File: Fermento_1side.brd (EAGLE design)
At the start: 85 x 68 mm, 25 parts, among them Q1 32.768kHz, Q2 P-MOSFET

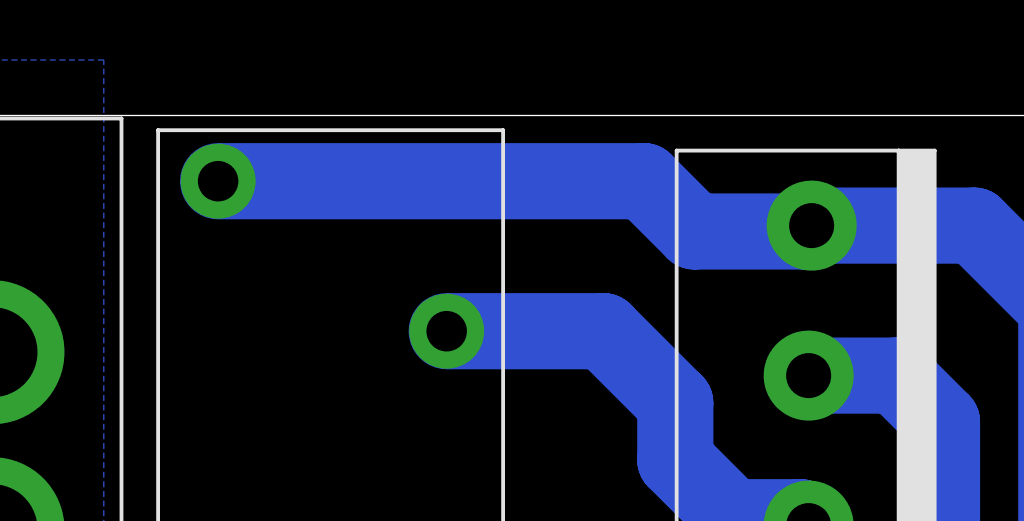
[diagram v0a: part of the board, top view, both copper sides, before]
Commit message: Added 1 sided version and png images.
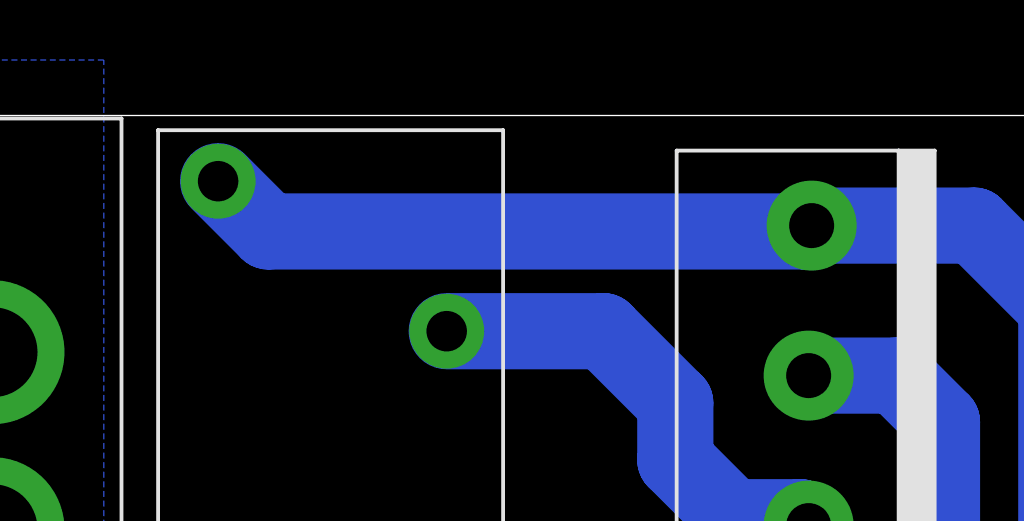
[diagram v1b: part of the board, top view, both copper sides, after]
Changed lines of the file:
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@@
 <wire x1="71.12" y1="44.45" x2="66.16" y2="44.45" width="2.54" layer="16"/>
 <wire x1="66.16" y1="44.45" x2="66.04" y2="44.33" width="2.54" layer="16"/>
-<wire x1="46.355" y1="65.81" x2="60.555" y2="65.81" width="2.54" layer="16"/>
-<wire x1="60.555" y1="65.81" x2="62.23" y2="64.135" width="2.54" layer="16"/>
-<wire x1="62.23" y1="64.135" x2="65.945" y2="64.135" width="2.54" layer="16"/>
 <wire x1="65.945" y1="64.135" x2="66.14" y2="64.33" width="2.54" layer="16"/>
 <wire x1="66.14" y1="64.33" x2="71.56" y2="64.33" width="2.54" layer="16"/>
+<wire x1="65.945" y1="64.135" x2="48.03" y2="64.135" width="2.54" layer="16"/>
+<wire x1="48.03" y1="64.135" x2="46.355" y2="65.81" width="2.54" layer="16"/>
 </signal>
 <signal name="N$8">

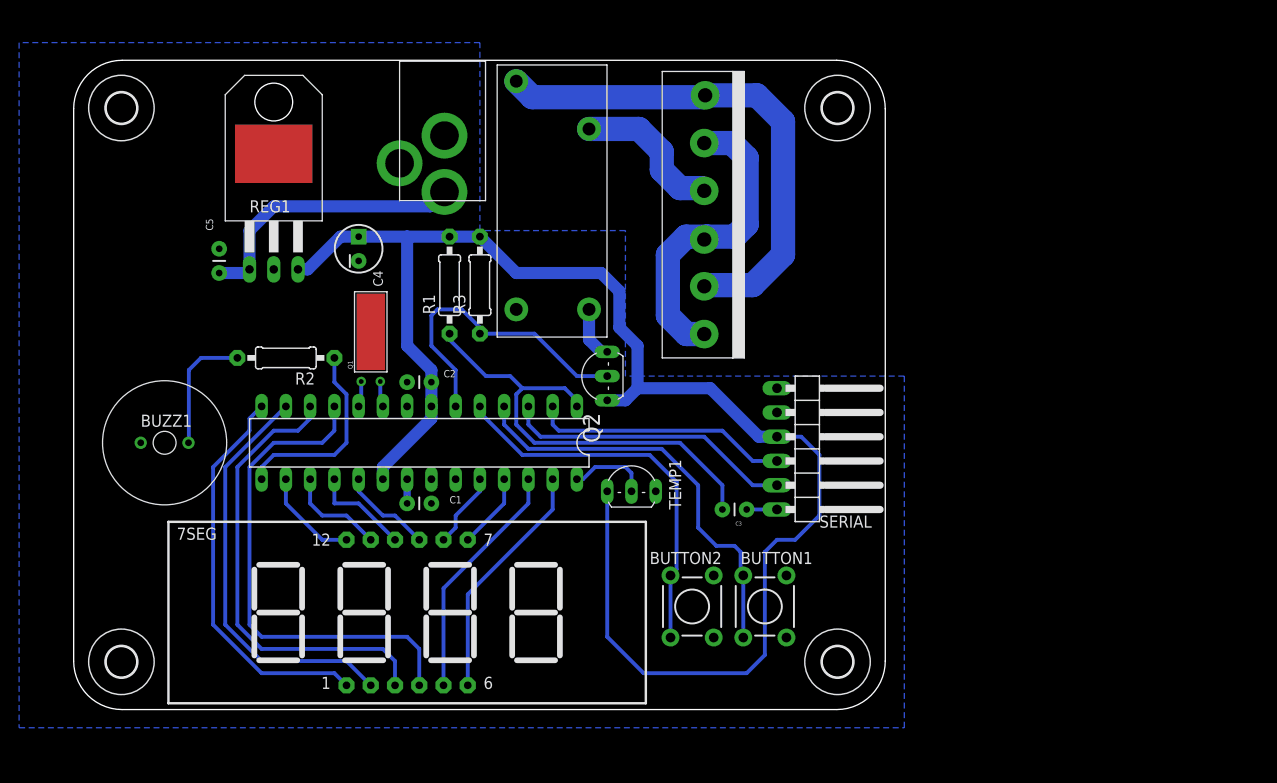
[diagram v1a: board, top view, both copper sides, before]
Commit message: Added mask and info diagram for 1sided homebrew incubator.
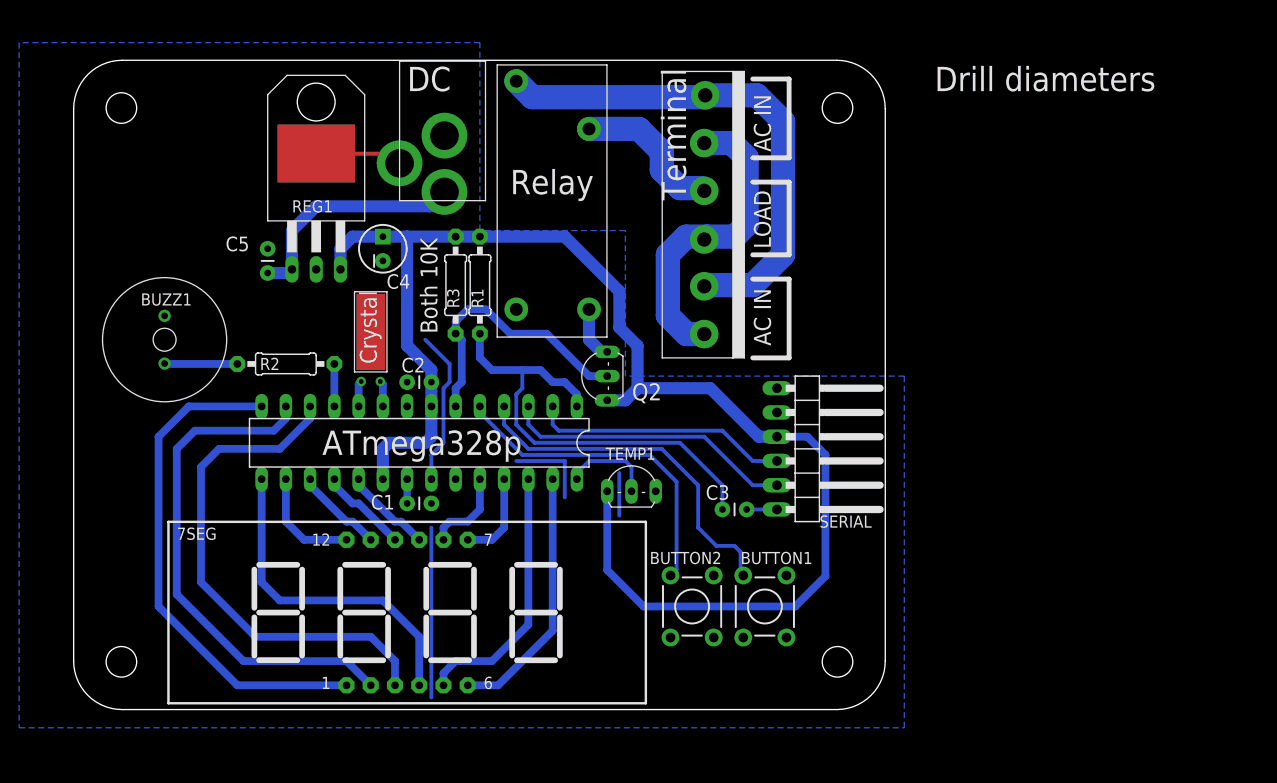
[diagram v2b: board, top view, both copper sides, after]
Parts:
- moved BUZZ1 10.8 mm to (9.53, 38.7), turned to 90 degrees
- moved C5 5.08 mm to (20.3, 45.7)
- moved REG1 4.45 mm to (20.3, 51.2)
- moved R1 3.18 mm to (42.5, 44.5)
- moved C4 2.54 mm to (32.4, 48.3)
- moved R3 2.54 mm to (40.0, 44.5)
- moved R2 0.63 mm to (22.2, 36.2)
- flipped H1 to the bottom
- flipped H2 to the bottom
- flipped H3 to the bottom
- flipped H4 to the bottom
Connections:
- net BUTTON1: no longer BUTTON1.1
- net BUTTON2: no longer BUTTON2.1
- net BUZZ: now also ATMEGA328.11; no longer ATMEGA328.15
- net C: now also ATMEGA328.15; no longer ATMEGA328.11
- net GND: no longer BUTTON1.3, BUTTON2.3
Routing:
- net GND: track 0.00 -> 56.7 mm
- net C: track 52.2 -> 34.8 mm
- net BUZZ: track 20.6 -> 4.45 mm
- net VCC: track 161.1 -> 149.0 mm
- net E: track 41.6 -> 53.0 mm
- net D: track 43.4 -> 53.5 mm
- net BUTTON2: track 40.8 -> 34.3 mm
- net BUTTON1: track 43.9 -> 37.4 mm
- net N$13: track 13.2 -> 7.64 mm
- net N$3: track 29.5 -> 24.4 mm
- net DP: track 48.1 -> 53.1 mm
- net AC_RELAY: track 32.5 -> 28.7 mm
- net G: track 25.3 -> 27.5 mm
- net DIG4: track 25.3 -> 27.1 mm
- net B: track 7.93 -> 9.42 mm
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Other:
- board text added: "AC IN"
- board text added: "ATmega328p"
- board text added: "All other drills: 0.9mm"
- board text added: "Both 10K"
- board text added: "Buttons: 1mm"
- board text added: "Buzzer+Crystal: 0.5mm"
- board text added: "Crystal"
- board text added: "DC"
- board text added: "DC Jack: 3mm"
- board text added: "Drill diameters"
- board text added: "LOAD"
- board text added: "Mount Holes: 3.2mm"
- board text added: "Regulator: 4mm"
- board text added: "Relay"
- board text added: "Relay: 1.35mm"
- board text added: "Terminal"
- board text added: "Terminal: 1.5mm"

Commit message: One sided homebrew-friendly design redone.
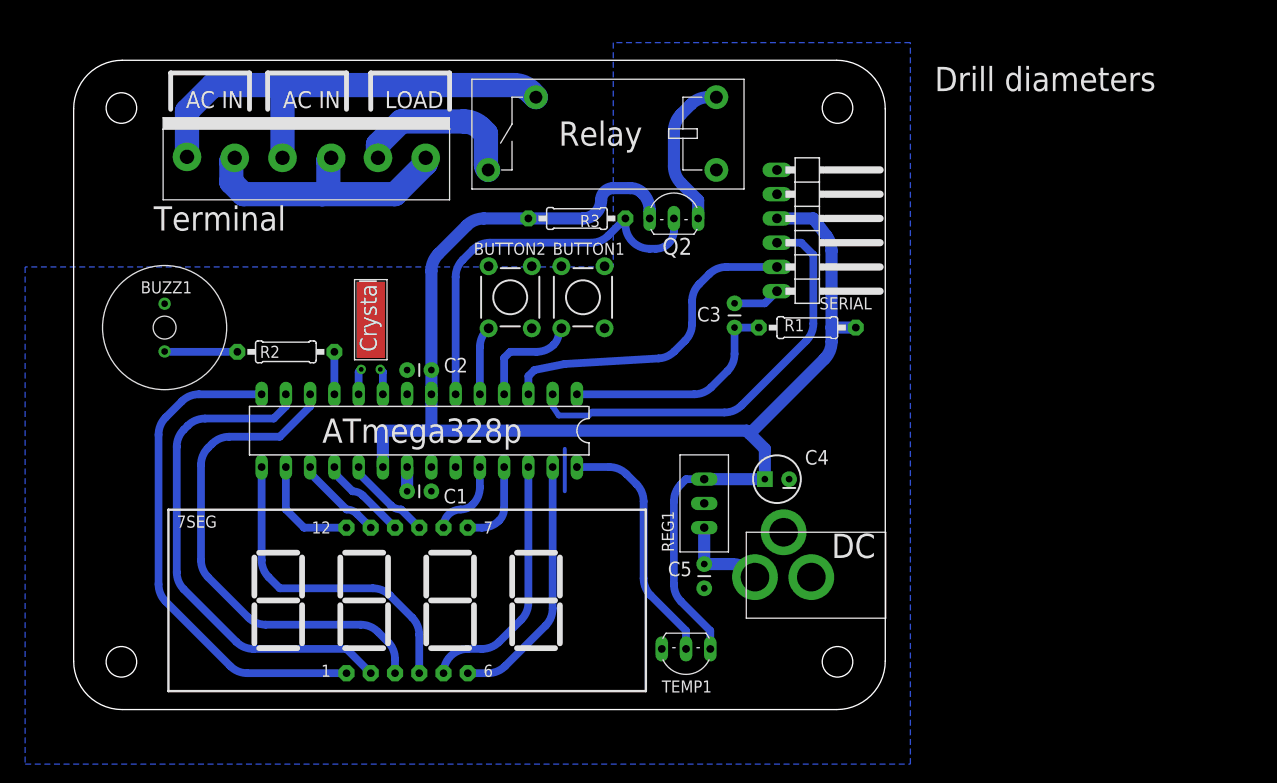
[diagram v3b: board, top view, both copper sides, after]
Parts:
- REG1: value TA48M033F -> (none); device Robin:TO-220 -> Robin:TO-220-STRAIGHT
- moved DC_JACK 64.9 mm to (80.6, 14.0), turned to 270 degrees
- moved C5 54.9 mm to (66.0, 15.2), turned to 270 degrees
- moved REG1 54.5 mm to (66.0, 21.6), turned to 90 degrees
- moved C4 47.8 mm to (73.7, 24.1), turned to 180 degrees
- moved BUTTON1 37.6 mm to (53.3, 43.2)
- moved BUTTON2 37.6 mm to (45.7, 43.2)
- moved R1 34.6 mm to (76.8, 40.0), turned to 0 degrees
- moved U$2 33.9 mm to (39.4, 57.8), turned to 180 degrees
- moved AC_RELAY 25.5 mm to (67.3, 56.5), turned to 180 degrees
- moved SERIAL 22.9 mm to (77.5, 50.2)
- moved C3 21.6 mm to (69.2, 42.5), turned to 270 degrees
- moved Q2 17.9 mm to (62.9, 51.4), turned to 0 degrees
- moved TEMP1 17.5 mm to (64.1, 6.35), turned to 180 degrees
- moved R3 14.5 mm to (52.7, 51.4), turned to 180 degrees
- moved BUZZ1 1.27 mm to (9.53, 40.0)
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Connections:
- net N$5 renamed AC1
- removed net N$6: AC_RELAY.3, U$2.2, U$2.6
- removed net N$8: AC_RELAY.2, U$2.4
- new net LOAD1: AC_RELAY.3, U$2.2
- new net LOAD2: AC_RELAY.2, U$2.4, U$2.6
- net BUTTON1: now also BUTTON1.1; no longer BUTTON1.2
- net BUTTON2: now also BUTTON2.1; no longer BUTTON2.2
- net GND: now also BUTTON1.3, BUTTON2.3; no longer REG1.THERMAL
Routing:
- net N$6: track 53.4 -> 0.00 mm
- net GND: track 56.7 -> 4.45 mm
- net LOAD2: track 0.00 -> 50.6 mm
- net BUTTON2: track 34.3 -> 7.13 mm
- net BUTTON1: track 37.4 -> 11.4 mm
- net RESET: track 48.3 -> 23.9 mm
- net RXI: track 27.0 -> 44.9 mm
- net LOAD1: track 0.00 -> 17.9 mm
- net TEMP_SENSE: track 9.68 -> 26.5 mm
- net N$8: track 15.9 -> 0.00 mm
- net N$3: track 24.4 -> 9.53 mm
- net AC_RELAY: track 28.7 -> 41.6 mm
- net RELAY: track 5.61 -> 16.2 mm
- net VCC: track 149.0 -> 154.1 mm
- net TXO: track 30.6 -> 34.2 mm
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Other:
- board text added: "C1,C2,C3: 0.1uF"
- board text added: "R1,R3: 10K"
- board text added: "R2: 1K"
- board text removed: "Both 10K"

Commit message: Added firmware to the repo.
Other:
- board text added: "C1,C2,C3,C5: 0.1uF"
- board text added: "C4: 47uF"
- board text removed: "C1,C2,C3: 0.1uF"
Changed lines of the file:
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@@
 <grid distance="0.025" unitdist="inch" unit="inch" style="dots" multiple="1" display="yes" altdistance="0.025" altunitdist="inch" altunit="inch"/>
 <layers>
-<layer number="1" name="Top" color="4" fill="1" visible="yes" active="yes"/>
+<layer number="1" name="Top" color="4" fill="1" visible="no" active="yes"/>
 <layer number="16" name="Bottom" color="1" fill="1" visible="yes" active="yes"/>
 <layer number="17" name="Pads" color="2" fill="1" visible="yes" active="yes"/>
@@
 <layer number="21" name="tPlace" color="7" fill="1" visible="yes" active="yes"/>
 <layer number="22" name="bPlace" color="7" fill="1" visible="yes" active="yes"/>
-<layer number="23" name="tOrigins" color="15" fill="1" visible="yes" active="yes"/>
-<layer number="24" name="bOrigins" color="15" fill="1" visible="yes" active="yes"/>
+<layer number="23" name="tOrigins" color="15" fill="1" visible="no" active="yes"/>
+<layer number="24" name="bOrigins" color="15" fill="1" visible="no" active="yes"/>
 <layer number="25" name="tNames" color="7" fill="1" visible="yes" active="yes"/>
 <layer number="26" name="bNames" color="7" fill="1" visible="no" active="yes"/>
@@
 <text x="90.17" y="26.67" size="1.778" layer="51">R1,R3: 10K</text>
 <text x="90.17" y="23.495" size="1.778" layer="51">R2: 1K</text>
-<text x="90.17" y="20.32" size="1.778" layer="51">C1,C2,C3: 0.1uF</text>
+<text x="90.17" y="20.32" size="1.778" layer="51">C1,C2,C3,C5: 0.1uF</text>
+<text x="90.17" y="17.145" size="1.778" layer="51">C4: 47uF</text>
 </plain>
 <attributes>
